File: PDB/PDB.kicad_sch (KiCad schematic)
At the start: 42 parts, among them Q1 S8050, Sw1 D-SWITCH_MR5-111-C5N-BB

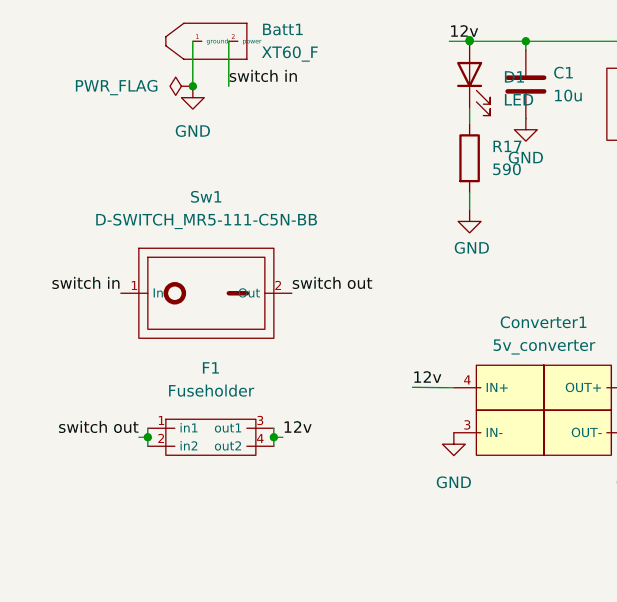
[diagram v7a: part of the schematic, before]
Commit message: Put most components on board
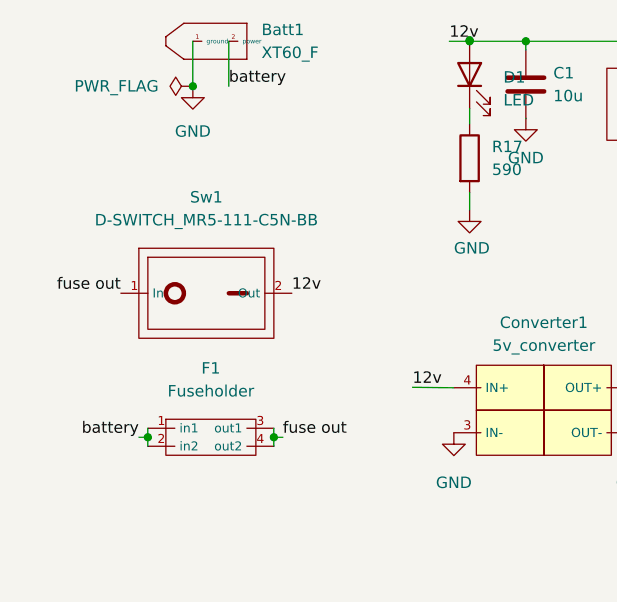
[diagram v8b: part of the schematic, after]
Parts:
- D1, D2: footprint LED_SMD:LED_0201_0603Metric -> LED_SMD:LED_0603_1608Metric
- Q1: footprint Package_TO_SOT_THT:TO-92_Inline -> PiE_Footprints:s8050 SMD
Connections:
- net 12v: now also Sw1.2 (Out); no longer F1.3 (out1), F1.4 (out2)
- net switch in renamed battery
- net battery: now also F1.1 (in1), F1.2 (in2); no longer Sw1.1 (In)
- removed net switch out: F1.1 (in1), F1.2 (in2), Sw1.2 (Out)
- new net fuse out: F1.3 (out1), F1.4 (out2), Sw1.1 (In)
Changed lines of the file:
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@@
     (effects (font (size 1.27 1.27)) (justify right bottom))
   )
-  (label "switch in" (at 33 22 0)
+  (label "battery" (at 33 22 0)
     (effects (font (size 1.27 1.27)) (justify left bottom))
   )
@@
     (effects (font (size 1.27 1.27)) (justify right bottom))
   )
-  (label "switch in" (at 21 45 180)
+  (label "fuse out" (at 21 45 180)
     (effects (font (size 1.27 1.27)) (justify right bottom))
   )
@@
     (effects (font (size 1.27 1.27)) (justify right bottom))
   )
-  (label "12v" (at 39 61 0)
+  (label "fuse out" (at 39 61 0)
     (effects (font (size 1.27 1.27)) (justify left bottom))
   )
@@
     (effects (font (size 1.27 1.27)) (justify right bottom))
   )
-  (label "switch out" (at 23 61 180)
+  (label "battery" (at 23 61 180)
     (effects (font (size 1.27 1.27)) (justify right bottom))
   )
@@
     (effects (font (size 1.27 1.27)) (justify left bottom))
   )
-  (label "switch out" (at 40 45 0)
+  (label "12v" (at 40 45 0)
     (effects (font (size 1.27 1.27)) (justify left bottom))
   )
@@
       (effects (font (size 1.27 1.27)) (justify right))
     )
-    (property "Footprint" "LED_SMD:LED_0201_0603Metric" (id 2) (at 105.75 51.44 0)
+    (property "Footprint" "LED_SMD:LED_0603_1608Metric" (id 2) (at 105.75 51.44 0)
       (effects (font (size 1.27 1.27)) hide)
     )
@@
       (effects (font (size 1.27 1.27)) (justify right))
     )
-    (property "Footprint" "LED_SMD:LED_0201_0603Metric" (id 2) (at 59.75 20.69 0)
+    (property "Footprint" "LED_SMD:LED_0603_1608Metric" (id 2) (at 59.75 20.69 0)
       (effects (font (size 1.27 1.27)) hide)
     )
@@
       (effects (font (size 1.27 1.27)) (justify left))
     )
-    (property "Footprint" "Package_TO_SOT_THT:TO-92_Inline" (id 2) (at 138.43 149.225 0)
+    (property "Footprint" "PiE_Footprints:s8050 SMD" (id 2) (at 138.43 149.225 0)
       (effects (font (size 1.27 1.27) italic) (justify left) hide)
     )
@@
     )
     (path "/90bd88d5-8304-4e21-8492-91fc773425c0"
-      (reference "D1") (unit 1) (value "LED") (footprint "LED_SMD:LED_0201_0603Metric")
+      (reference "D1") (unit 1) (value "LED") (footprint "LED_SMD:LED_0603_1608Metric")
     )
     (path "/60da32c4-832f-4d02-a76f-09bc060801f0"
-      (reference "D2") (unit 1) (value "LED") (footprint "LED_SMD:LED_0201_0603Metric")
+      (reference "D2") (unit 1) (value "LED") (footprint "LED_SMD:LED_0603_1608Metric")
     )
     (path "/1e084e26-6ae1-49d5-9c52-b72c77647dd7"
@@
     )
     (path "/92a8788b-cd93-4edc-bbd4-f4c805195988"
-      (reference "Q1") (unit 1) (value "S8050") (footprint "Package_TO_SOT_THT:TO-92_Inline")
+      (reference "Q1") (unit 1) (value "S8050") (footprint "PiE_Footprints:s8050 SMD")
     )
     (path "/033d6a7e-9f33-4dd9-ba87-8880049ad6d6"
